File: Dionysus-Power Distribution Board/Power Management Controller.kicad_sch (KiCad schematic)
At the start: 122 parts

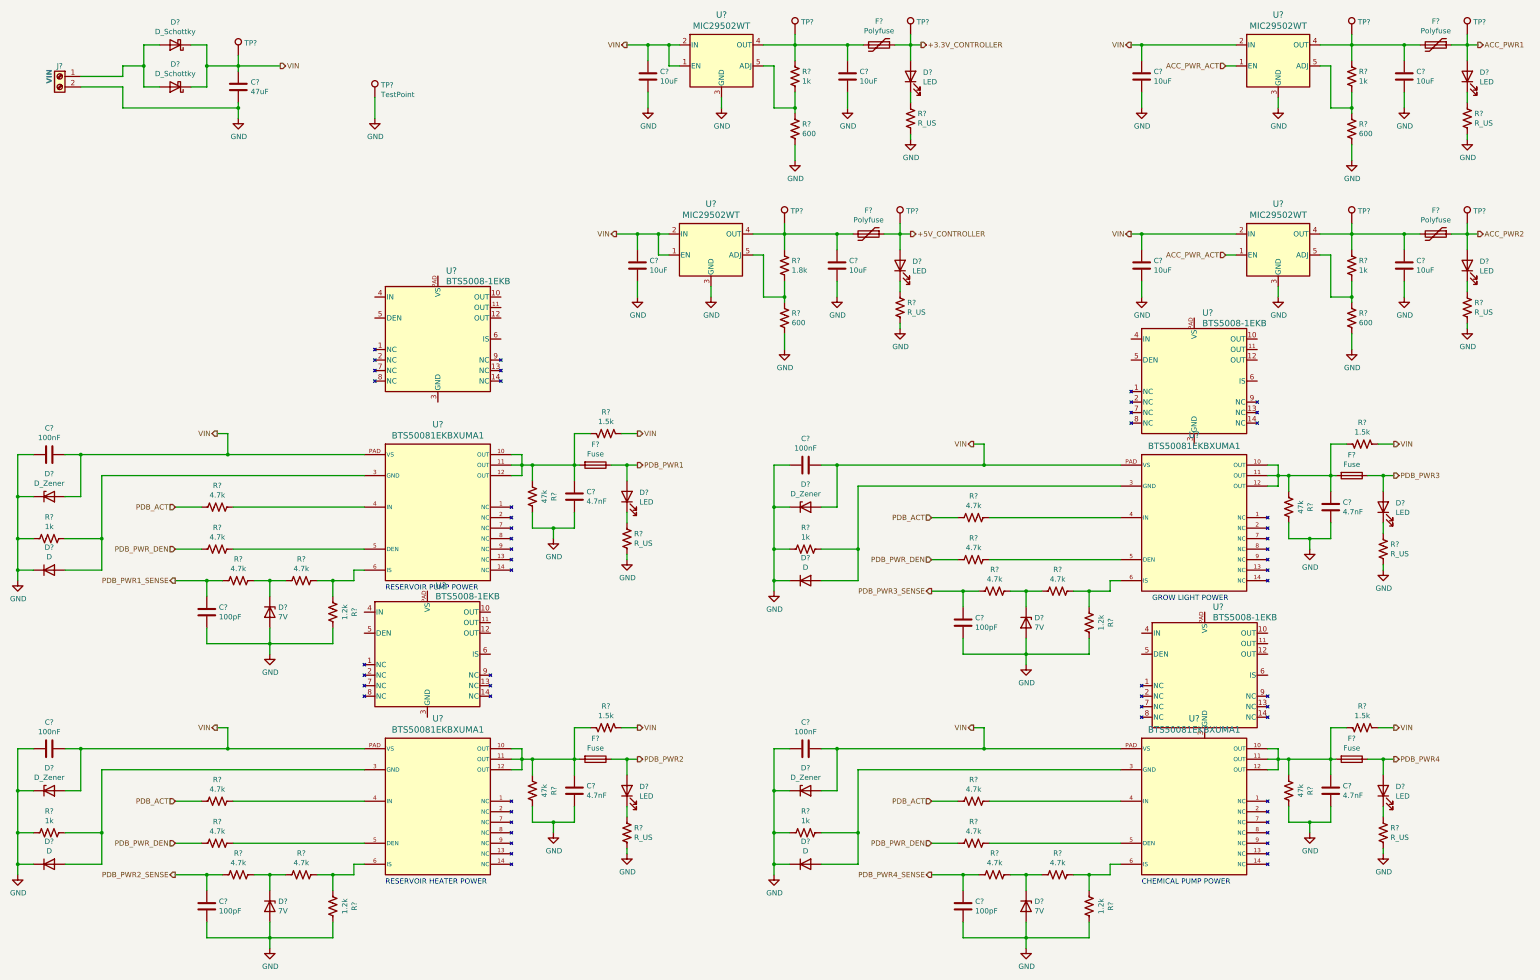
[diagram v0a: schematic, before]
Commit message: Updated Symbols and Redefined Hierarchical Pins
Updated high side driver symbols, and added hierarchical pins to page 1
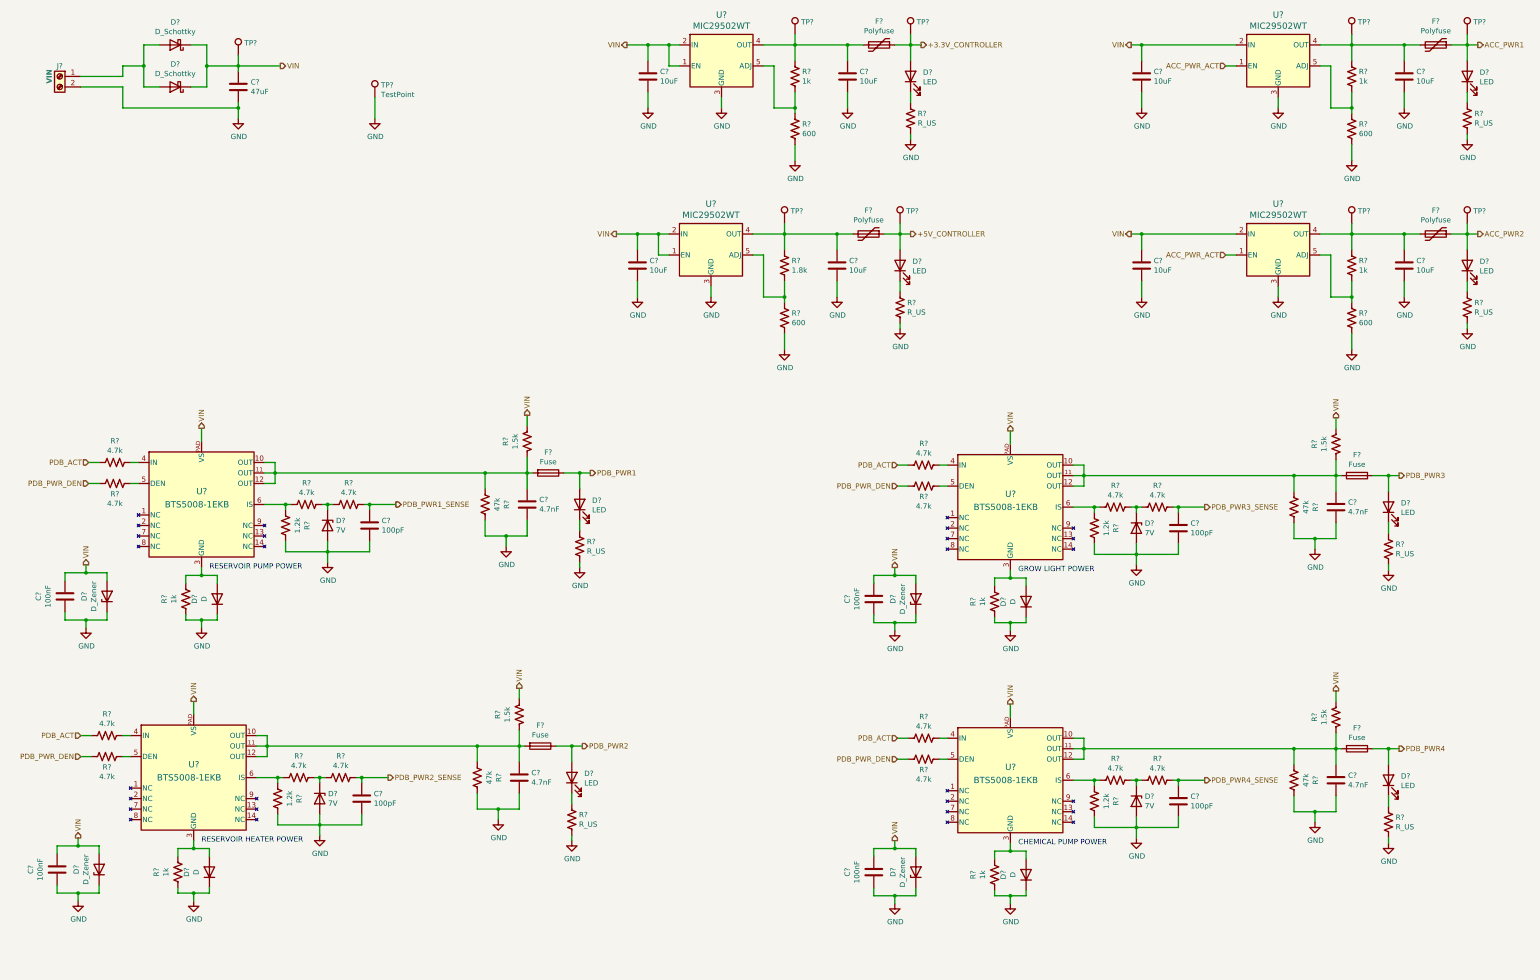
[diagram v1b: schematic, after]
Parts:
- removed C? (x3): 4.7nF, symbol Device:C
- removed C? (x3): 100nF, symbol Device:C
- removed C? (x3): 100pF, symbol Device:C
- removed D? (x3): D_Zener, symbol Device:D_Zener
- removed D? (x3): D, symbol Device:D
- removed D? (x3): LED, symbol Device:LED
- removed D? (x3): 7V, symbol Device:D_Zener
- removed F? (x3): Fuse, symbol Device:Fuse
- removed R? (x3): 47k, symbol Device:R_US
- removed R? (x12): 4.7k, symbol Device:R_US
- removed R? (x3): 1k, symbol Device:R_US
- removed R? (x3): R_US, symbol Device:R_US
- removed R? (x3): 1.5k, symbol Device:R_US
- removed R? (x3): 1.2k, symbol Device:R_US
- removed U? (x3): BTS5008-1EKB, PG-DSO-14-47-EP_INF, symbol Driver_Load_jal:BTS5008-1EKB
- removed U? (x4): BTS50081EKBXUMA1, PG-DSO-14-47-EP_INF, symbol Power Distribution Board-rescue:BTS50081EKBXUMA1-Driver_Load
- added C? (x3): 100nF, symbol Device:C
- added C? (x3): 100pF, symbol Device:C
- added C? (x3): 4.7nF, symbol Device:C
- added D? (x3): 7V, symbol Device:D_Zener
- added D? (x3): D_Zener, symbol Device:D_Zener
- added D? (x3): LED, symbol Device:LED
- added D? (x3): D, symbol Device:D
- added F? (x3): Fuse, symbol Device:Fuse
- added R? (x12): 4.7k, symbol Device:R_US
- added R? (x3): R_US, symbol Device:R_US
- added R? (x3): 47k, symbol Device:R_US
- added R? (x3): 1.2k, symbol Device:R_US
- added R? (x3): 1k, symbol Device:R_US
- added R? (x3): 1.5k, symbol Device:R_US
- added U? (x3): BTS5008-1EKB, PG-DSO-14-47-EP_INF, symbol Driver_Load_jal:BTS5008-1EKB
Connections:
- net GND: now also C?.2, C?.2, C?.2, C?.2, C?.2, C?.2, C?.2, C?.2, C?.2, D?.1 (K), D?.1 (K), D?.1 (K), D?.1 (K), D?.1 (K), D?.1 (K), D?.2 (A), D?.2 (A), D?.2 (A), R?.1, R?.1, R?.1, R?.1, R?.1, R?.1, R?.2, R?.2, R?.2, R?.2, R?.2, R?.2
- net PDB_ACT: now also R?.2, R?.2, R?.2
- net PDB_PWR1_SENSE: now also R?.1; no longer R?.2
- net PDB_PWR2: now also D?.2 (A), F?.1
- net PDB_PWR2_SENSE: now also C?.1, R?.1
- net PDB_PWR3: now also D?.2 (A), F?.1
- net PDB_PWR3_SENSE: now also C?.1, R?.1
- net PDB_PWR4: now also D?.2 (A), F?.1
- net PDB_PWR4_SENSE: now also C?.1, R?.1
- net PDB_PWR_DEN: now also R?.2, R?.2, R?.2
- net VIN: now also U?.PAD (VS), C?.1, C?.1, C?.1, D?.2 (A), D?.2 (A), D?.2 (A), R?.2, R?.2, R?.2, U?.PAD (VS), U?.PAD (VS), U?.PAD (VS)
- net at C?.1, F?.2, R?.1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: now also U?.10 (OUT), U?.11 (OUT), U?.12 (OUT)
- net at D?.2 (A), R?.1: now also U?.3 (GND)
- net at R?.2: now also R?.2, U?.6 (IS); no longer R?.1
- net at U?.4 (IN): now also R?.1
- net at U?.5 (DEN): now also R?.1
- new net: D?.1 (K), R?.1, R?.2 (x3)
- new net: D?.1 (K), R?.1 (x3)
- new net: R?.2, R?.2, U?.6 (IS) (x3)
- new net: C?.1, F?.2, R?.1, R?.2, U?.10 (OUT), U?.11 (OUT), U?.12 (OUT) (x3)
- new net: D?.2 (A), R?.1, U?.3 (GND) (x3)
- new net: R?.1, U?.4 (IN) (x3)
- new net: R?.1, U?.5 (DEN) (x3)
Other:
- moved on the sheet: C?, D?, F?, R?, U?
